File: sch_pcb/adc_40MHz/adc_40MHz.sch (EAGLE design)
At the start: 63 parts, among them IC1 LTC2227, IC2 LT6600-15, IC3 LTC6254XMS, IC5 LT1521XST, X1 SIGNAL, X2 CLK

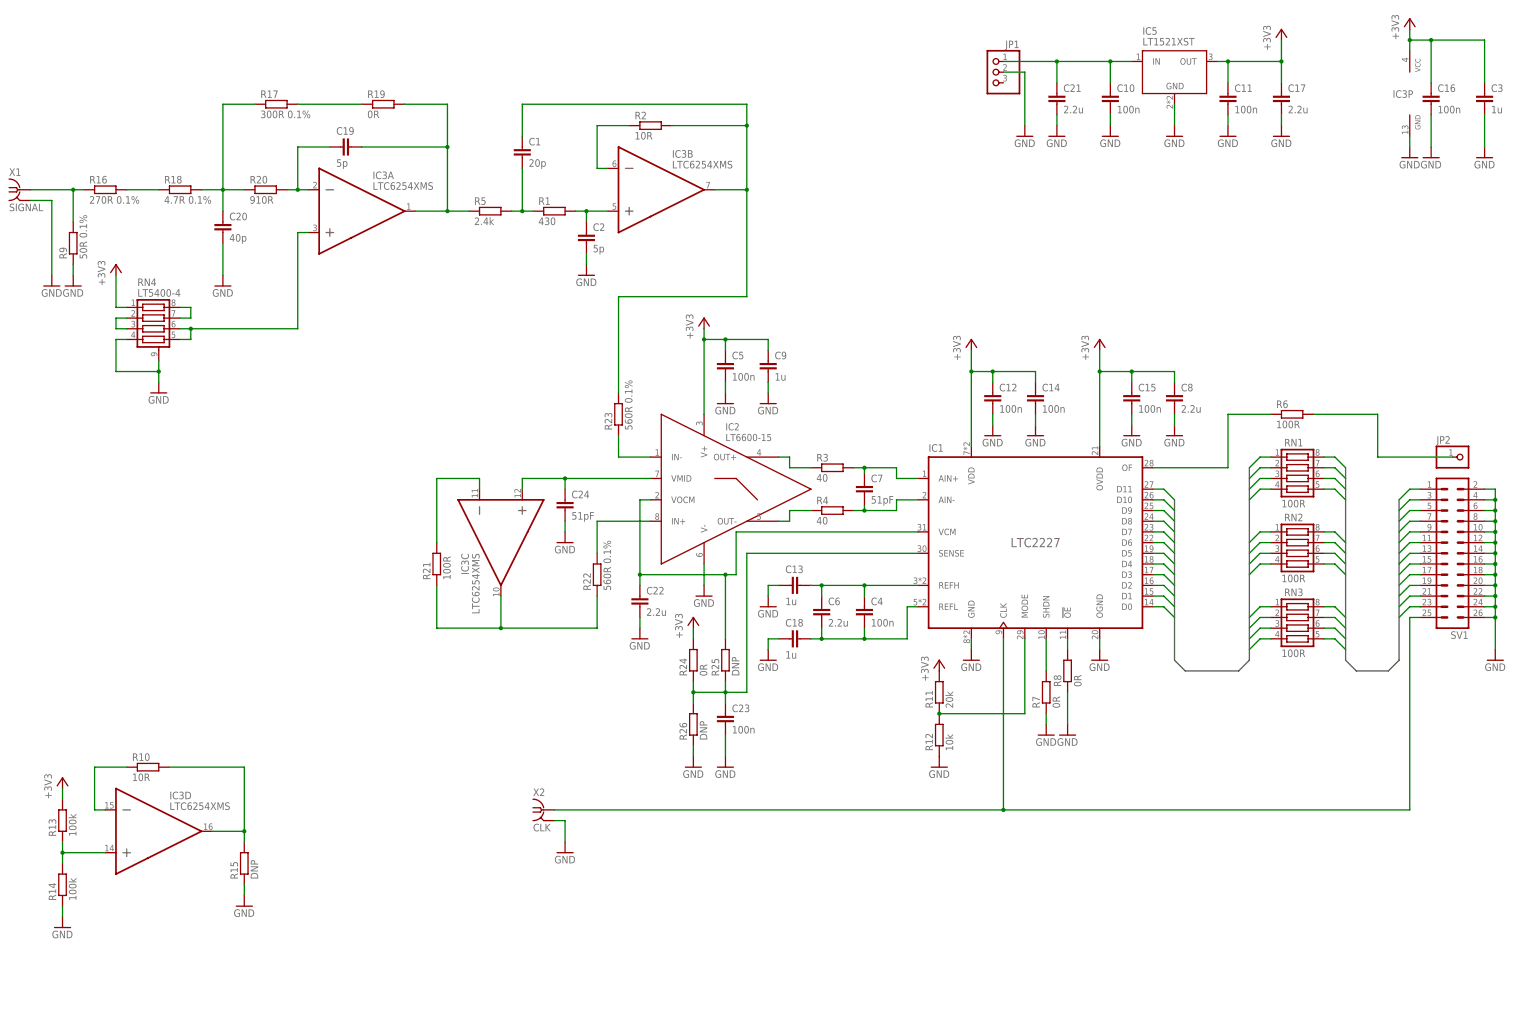
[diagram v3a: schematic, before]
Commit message: Dokonczono model inwertera. Dodano go na schemat. Przed zmiana przetwornika na AD9235
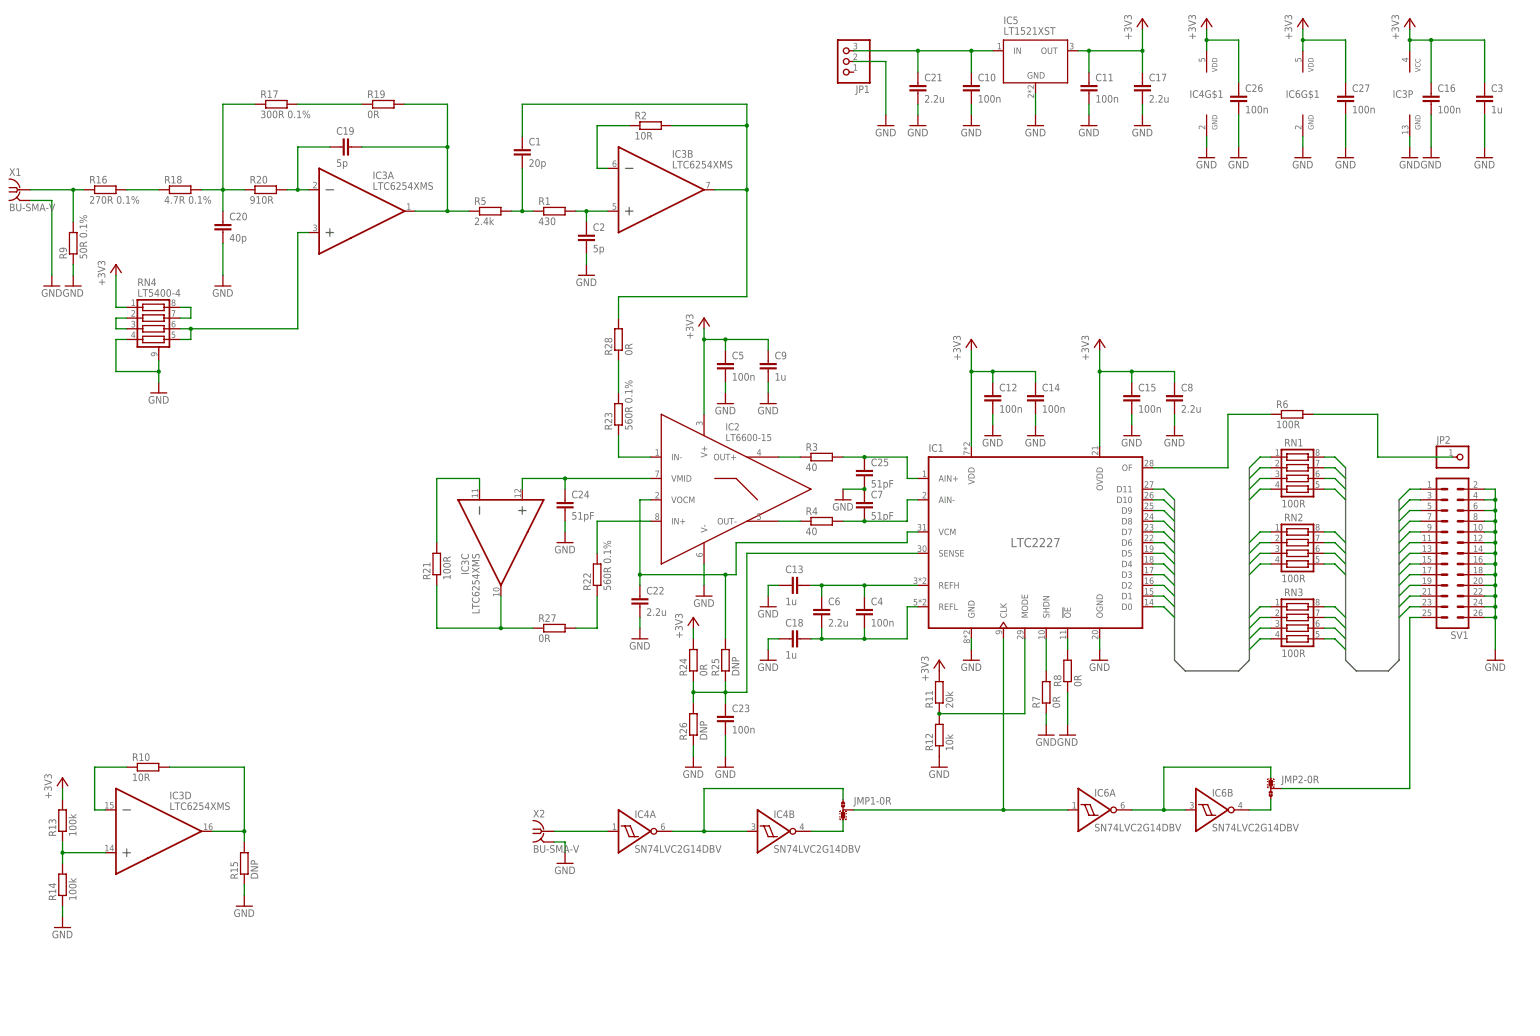
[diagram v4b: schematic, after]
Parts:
- added C25: 51pF, rcl:C-EUC0603
- added C26, C27: 100n, rcl:C-EUC0805
- added IC4, IC6: SN74LVC2G14DBV, sn74lvc2g14:SN74LVC2G14DBV
- added JMP1, JMP2: 0R-JUMPA, jump-0r-smd:0R-JUMPA
- added R27, R28: 0R, rcl:R-EU_R0603
- X1: value SIGNAL -> BU-SMA-V; device con-coax:BU-SMA-H -> con-coax:BU-SMA-V
- X2: value CLK -> BU-SMA-V; device con-coax:BU-SMA-H -> con-coax:BU-SMA-V
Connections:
- new net N$34: IC4A.I, X2.1
- new net N$36: IC4A.O, IC4B.I, JMP1-0R.1
- new net N$37: IC1.CLK, IC6A.I, JMP1-0R.2
- new net N$38: IC6A.O, IC6B.I, JMP2-0R.1
- new net N$39: IC4B.O, JMP1-0R.3
- new net N$40: R23.2, R28.1
- new net N$41: IC6B.O, JMP2-0R.3
- new net N$42: R22.1, R27.2
- net +3V3: now also C26.1, C27.1, IC4G$1.V+, IC6G$1.V+
- net CLK: now also JMP2-0R.2; no longer IC1.CLK, X2.1
- net GND: now also C25.2, C26.2, C27.2, C7.1, IC4G$1.V-, IC6G$1.V-
- net N$13: now also R27.1; no longer R22.1
- net N$2: now also C25.1; no longer C7.1
- net N$27: now also R28.2; no longer R23.2
- net VIN: now also JP1.3; no longer JP1.1
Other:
- moved on the sheet: C10, C11, C17, C21, C7, IC5, JP1, R3, R4, X2

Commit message: Skończony (chyba) schemat dla nowego ADC i rozpoczęte układanie płytki
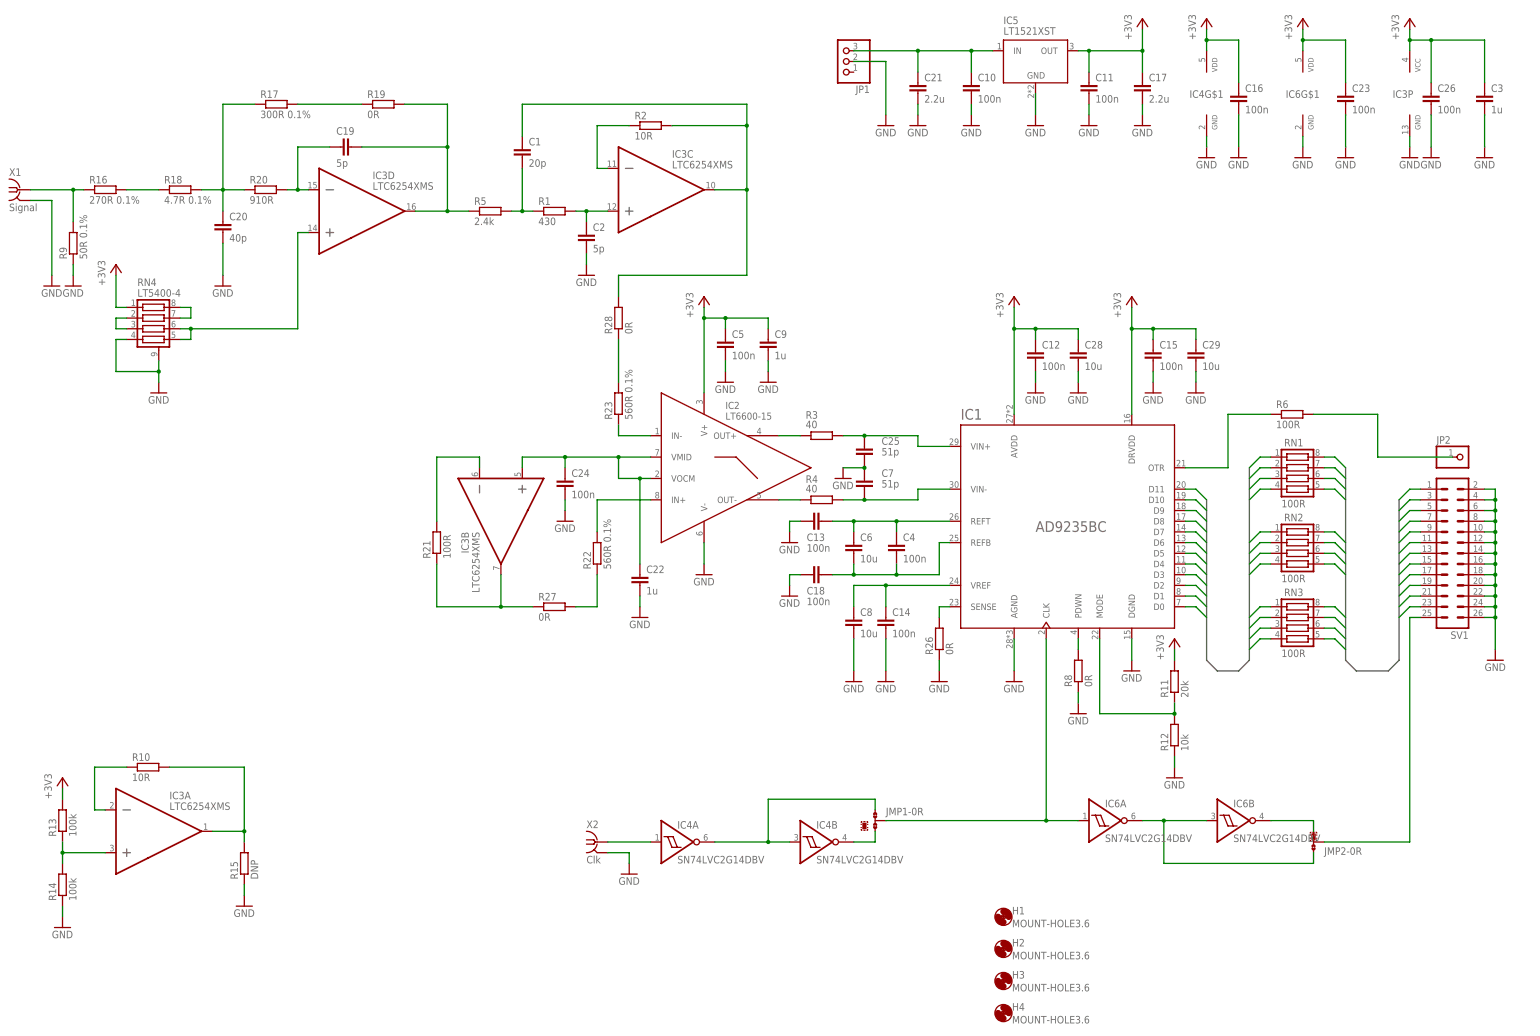
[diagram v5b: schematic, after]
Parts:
- removed C27: 100n, rcl:C-EUC0805
- removed R24, R7: 0R, rcl:R-EU_R0603
- removed R25: DNP, rcl:R-EU_R0603
- added C28, C29: 10u, rcl:C-EUC1206
- added H1, H2, H3, H4: MOUNT-HOLE3.6, holes:MOUNT-HOLE3.6
- C10, C11, C16, C26: device rcl:C-EUC0805 -> rcl:C-EUC0603
- C13, C18: value 1u -> 100n; device rcl:C-EUC0805 -> rcl:C-EUC0603
- C22: value 2.2u -> 1u
- C24: value 51pF -> 100n
- C25, C7: value 51pF -> 51p
- C6, C8: value 2.2u -> 10u; device rcl:C-EUC0805 -> rcl:C-EUC1206
- IC1: value LTC2227 -> AD9235BC; device ltc22xx:LTC2227 -> ad9235:AD9235BC
- R26: value DNP -> 0R
- X1: value BU-SMA-V -> Signal
- X2: value BU-SMA-V -> Clk
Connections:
- removed net N$18: C24.1, IC2.VMID, IC3C.+IN
- net +3V3: now also C23.1, C28.1, C29.1, IC1.AVDD, IC1.DRVDD; no longer C14.1, C27.1, C8.1, IC1.OVDD, IC1.VDD, R24.2
- net GND: now also C28.2, C29.2, IC1.AGND, IC1.DGND; no longer C27.2, IC1.GND, IC1.OGND, R7.1
- net N$10: now also C22.1, C24.1, IC2.VMID, IC2.VOCM, IC3B.+IN; no longer IC1.SHDN, R7.2
- net N$12: now also IC3A.+IN; no longer IC3D.+IN
- net N$13: now also IC3B.OUT; no longer IC3C.OUT
- net N$14: now also IC3A.-IN; no longer IC3D.-IN
- net N$15: now also IC3A.OUT; no longer IC3D.OUT
- net N$17: now also IC3B.-IN; no longer IC3C.-IN
- net N$2: now also IC1.VIN+; no longer IC1.AIN+
- net N$22: now also IC3D.OUT; no longer IC3A.OUT
- net N$23: now also IC3D.-IN; no longer IC3A.-IN
- net N$24: now also IC3D.+IN; no longer IC3A.+IN
- net N$26: now also IC3C.-IN; no longer IC3B.-IN
- net N$27: now also IC3C.OUT; no longer IC3B.OUT
- net N$29: now also IC3C.+IN; no longer IC3B.+IN
- net N$3: now also IC1.VIN-; no longer IC1.AIN-
- net N$33: now also IC1.REFT; no longer IC1.REFH
- net N$35: no longer C23.1, R24.1, R25.1
- net N$5: now also C14.1, C8.1, IC1.VREF; no longer C22.1, IC1.VCM, IC2.VOCM, R25.2
- net N$6: now also IC1.OTR; no longer IC1.OF
- net N$7: now also IC1.REFB; no longer IC1.REFL
- net N$9: now also IC1.PDWN; no longer IC1.!OE
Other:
- moved on the sheet: C12, C13, C14, C15, C16, C18, C22, C23, C24, C25, C26, C4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

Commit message: Poprawiono kondensatory przy LT6600. Częściowe połączenie ścieżek (pierwsze stopnie filtru)
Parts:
- C1, C10, C11, C12, C13, C14, C15, C16, C18, C19, C2, C20, C23, C25, C26, C4, C5, C7: device rcl:C-EUC0603 -> resistor:C-EUC0603K
- C22: value 1u -> 10n; device rcl:C-EUC0805 -> resistor:C-EUC0603K
- C24: value 100n -> 10n; device rcl:C-EUC0603 -> resistor:C-EUC0603K
- X1: value Signal -> SMA-142-0701-851/861; device con-coax:BU-SMA-V -> con-coax:SMA-142-0701-851/861
- X2: value Clk -> SMA-142-0701-851/861; device con-coax:BU-SMA-V -> con-coax:SMA-142-0701-851/861
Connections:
- removed net N$11: R16.1, R9.2, X1.1
- net VIN: now also R16.1, R9.2, X1.1
